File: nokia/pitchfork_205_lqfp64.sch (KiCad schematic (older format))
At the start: 71 parts, among them IC1 STM32F2XX_64LQFP, K1 CONN_3, U1 LM3670, U2 USBCONN, U3 MCP73832-2, U4 NRF24L01+, U5 MC74VHC1G66, U6 MICROSDCARD, U7 TSV912, U8 TC75W57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

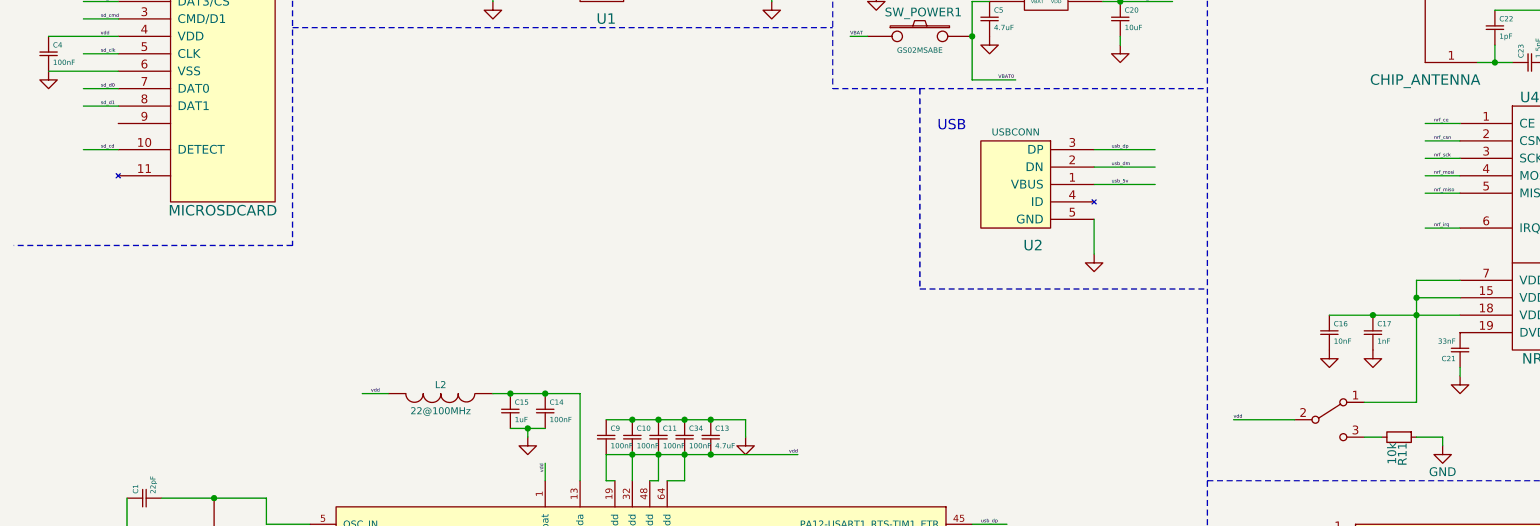
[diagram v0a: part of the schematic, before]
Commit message: [fix] added SD card detect GND pin to sch
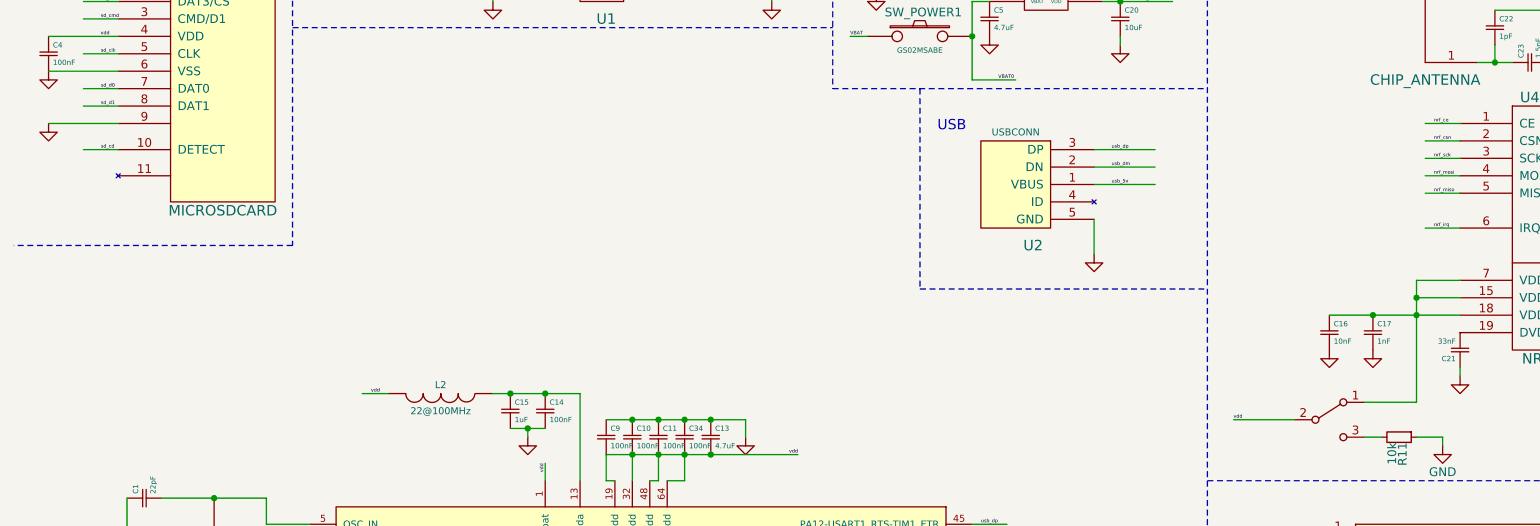
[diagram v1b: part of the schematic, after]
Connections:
- wire segments 320 -> 321
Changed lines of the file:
@@
 	8000 2750 8750 2750
 Wire Wire Line
-	8500 3250 8500 2550
+	8500 2550 8500 3250
 Connection ~ 8500 2650
 Connection ~ 8500 2750
@@
 	3000 700  3500 700
 Wire Wire Line
-	8200 3250 8500 3250
+	8500 3250 8200 3250
 Wire Wire Line
 	8200 3450 8300 3450
@@
 Wire Wire Line
 	8650 3450 8650 3500
+$Comp
+L GND #PWR?
+U 1 1 59051031
+P 650 1650
+F 0 "#PWR?" H 650 1650 30  0001 C CNN
+F 1 "GND" H 650 1580 30  0001 C CNN
+F 2 "" H 650 1650 60  0000 C CNN
+F 3 "" H 650 1650 60  0000 C CNN
+	1    650  1650
+	1    0    0    -1
+$EndComp
+Wire Wire Line
+	1050 1650 650  1650
 $EndSCHEMATC

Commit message: [mod] button schema beautified in nokia
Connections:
- wire segments 321 -> 409
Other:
- moved on the sheet: D2, D3, D4, D5, D6, D7, D8, D9
